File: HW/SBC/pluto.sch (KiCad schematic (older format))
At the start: 0 parts

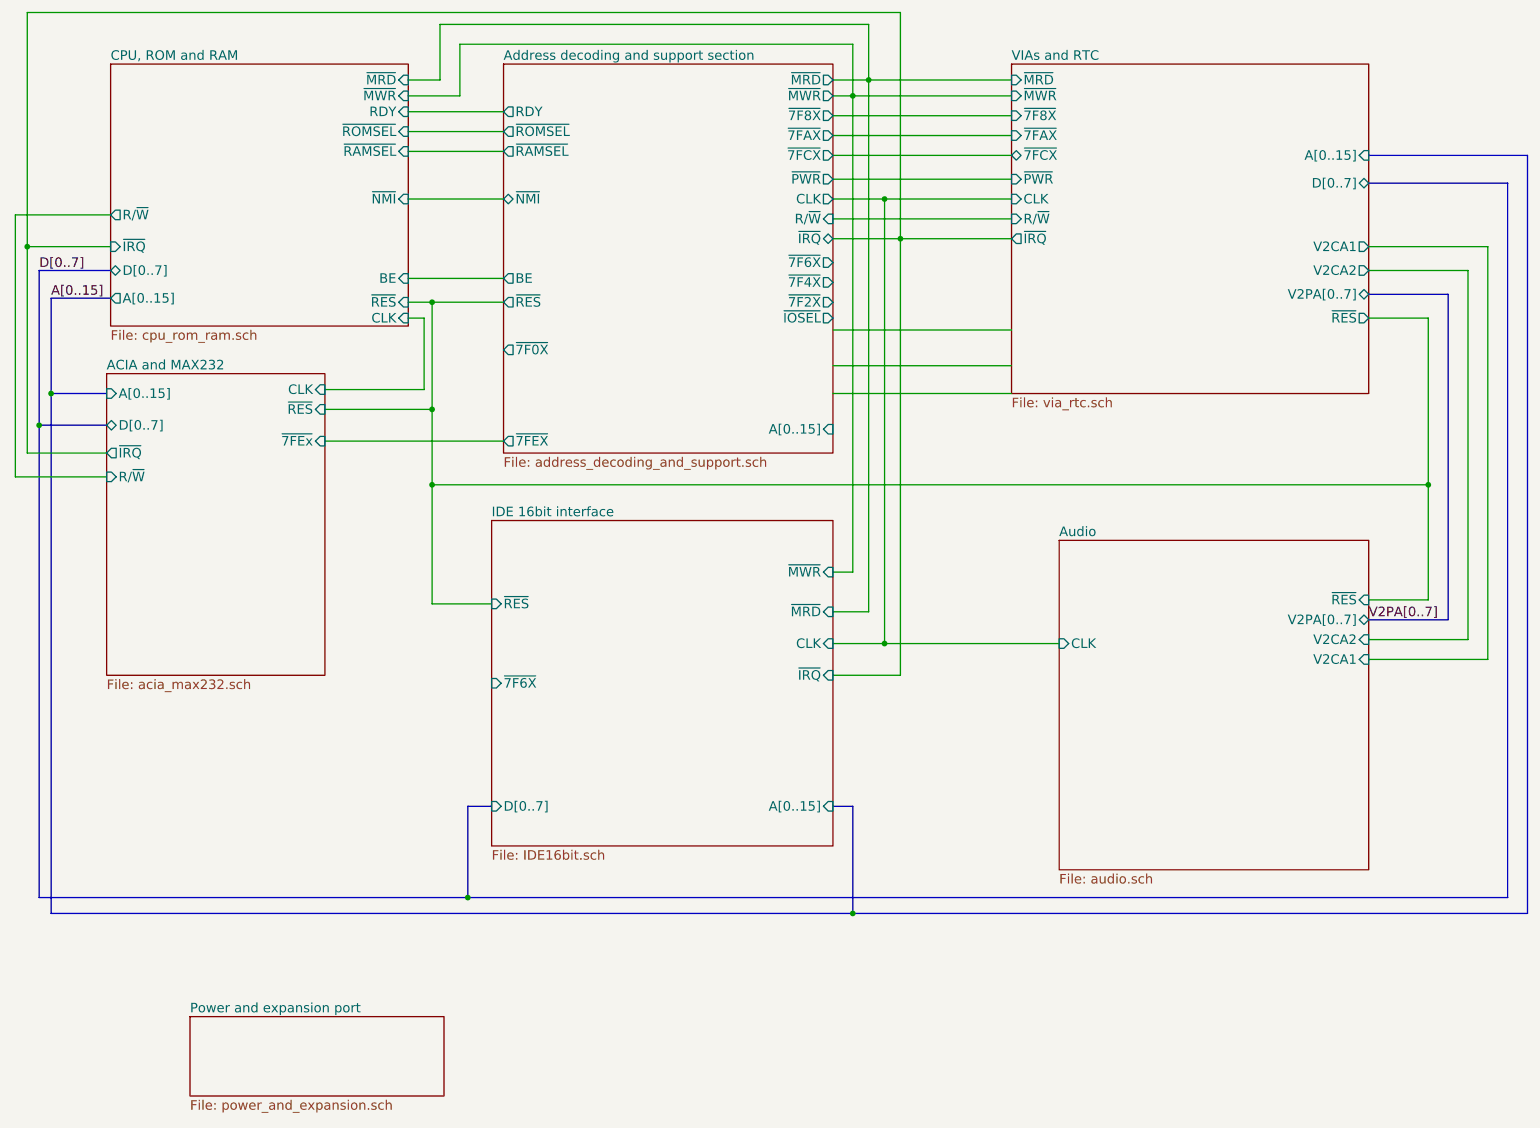
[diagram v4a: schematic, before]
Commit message: Still no VCC net in PCBnew.
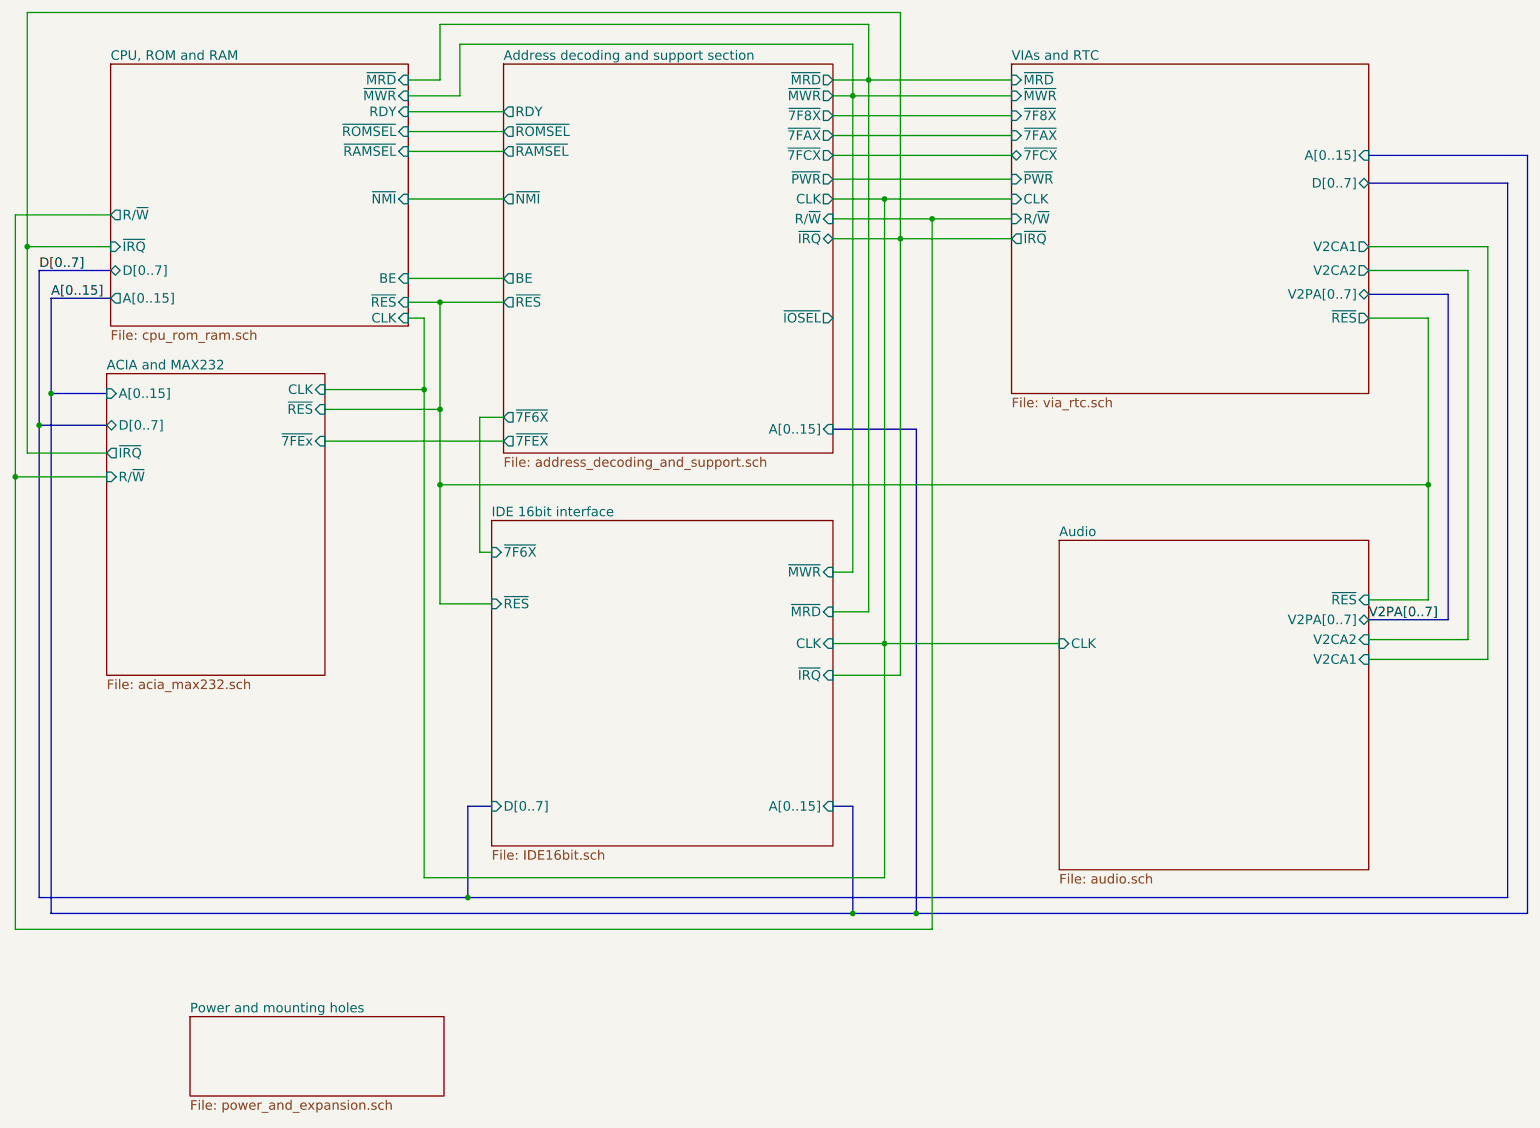
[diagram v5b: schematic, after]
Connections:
- wire segments 56 -> 59
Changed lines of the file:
@@
 EESchema Schematic File Version 2
-LIBS:pluto-rescue
 LIBS:power
 LIBS:device
@@
 LIBS:pluto
 LIBS:pluto-cache
-LIBS:IDE_interface-cache
 EELAYER 25 0
 EELAYER END
@@
 F7 "R/~W" O L 1350 1850 60
 F8 "~NMI" I R 3225 1750 60
-F9 "~RES" I R 3225 2400 60
-F10 "CLK" I R 3225 2500 60
-F11 "~MRD" I R 3225 1000 60
-F12 "~MWR" I R 3225 1100 60
-F13 "~RAMSEL" I R 3225 1450 60
-F14 "~ROMSEL" I R 3225 1325 60
+F9 "CLK" I R 3225 2500 60
+F10 "~MRD" I R 3225 1000 60
+F11 "~MWR" I R 3225 1100 60
+F12 "~RAMSEL" I R 3225 1450 60
+F13 "~ROMSEL" I R 3225 1325 60
+F14 "~RES" I R 3225 2400 60
 $EndSheet
 $Sheet
@@
 F9 "R/~W" I R 5900 1875 60
 F10 "~IRQ" B R 5900 2000 60
-F11 "~NMI" B L 3825 1750 60
+F11 "~NMI" O L 3825 1750 60
 F12 "BE" O L 3825 2250 60
 F13 "~PWR" O R 5900 1625 60
 F14 "RDY" O L 3825 1200 60
 F15 "~RES" O L 3825 2400 60
-F16 "~7F0X" O L 3825 2700 60
-F17 "~7F2X" O R 5900 2400 60
-F18 "~7F4X" O R 5900 2275 60
-F19 "~7F6X" O R 5900 2150 60
-F20 "~7F8X" O R 5900 1225 60
-F21 "~7FAX" O R 5900 1350 60
-F22 "~7FCX" O R 5900 1475 60
-F23 "~7FEX" O L 3825 3275 60
+F16 "~7F6X" O L 3825 3125 60
+F17 "~7F8X" O R 5900 1225 60
+F18 "~7FAX" O R 5900 1350 60
+F19 "~7FCX" O R 5900 1475 60
+F20 "~7FEX" O L 3825 3275 60
 $EndSheet
 $Sheet
 S 1850 6900 1600 500
 U 58D589DC
-F0 "Power and expansion port" 60
+F0 "Power and mounting holes" 60
 F1 "power_and_expansion.sch" 60
 $EndSheet
@@
 F1 "audio.sch" 60
 F2 "V2PA[0..7]" B R 9275 4400 60
-F4 "V2CA2" I R 9275 4525 60
-F5 "V2CA1" I R 9275 4650 60
-F6 "~RES" I R 9275 4275 60
-F7 "CLK" I L 7325 4550 60
-$EndSheet
-Wire Wire Line
-	5900 2800 7025 2800
-Wire Wire Line
-	5900 2975 7025 2975
-Wire Wire Line
-	5900 2575 7025 2575
+F3 "V2CA2" I R 9275 4525 60
+F4 "V2CA1" I R 9275 4650 60
+F5 "~RES" I R 9275 4275 60
+F6 "CLK" I L 7325 4550 60
+$EndSheet
 Wire Wire Line
 	5900 2000 7025 2000
@@
 F6 "CLK" I R 5900 4550 60
 F7 "~MRD" I R 5900 4350 60
-F8 "~7F6X" I L 3750 4800 60
+F8 "~7F6X" I L 3750 3975 60
 F9 "~MWR" I R 5900 4100 60
 $EndSheet
@@
 	3225 2500 3325 2500
 Wire Wire Line
-	3325 2500 3325 2950
+	3325 2500 3325 6025
 Wire Wire Line
 	3325 2950 2700 2950
@@
 	3225 2400 3825 2400
 Wire Wire Line
-	3375 2400 3375 4300
-Wire Wire Line
-	3375 3075 2700 3075
+	3425 2400 3425 4300
+Wire Wire Line
+	3425 3075 2700 3075
 Wire Wire Line
 	3225 2250 3825 2250
@@
 	1350 1850 750  1850
 Wire Wire Line
-	750  1850 750  3500
+	750  1850 750  6350
 Wire Wire Line
 	750  3500 1325 3500
@@
 	5900 4550 7325 4550
 Wire Wire Line
-	6225 1750 6225 4550
+	6225 1750 6225 6025
 Connection ~ 6225 4550
 Connection ~ 6225 1750
@@
 Wire Wire Line
 	6325 4750 5900 4750
-Connection ~ 3375 2400
-Wire Wire Line
-	3375 4300 3750 4300
-Connection ~ 3375 3075
-Wire Wire Line
-	3375 3550 9650 3550
+Connection ~ 3425 2400
+Wire Wire Line
+	3425 4300 3750 4300
+Connection ~ 3425 3075
+Wire Wire Line
+	3425 3550 9650 3550
 Connection ~ 9650 3550
-Connection ~ 3375 3550
+Connection ~ 3425 3550
 Wire Wire Line
 	3225 1750 3825 1750
+Wire Wire Line
+	3825 3125 3675 3125
+Wire Wire Line
+	3675 3125 3675 3975
+Wire Wire Line
+	3675 3975 3750 3975
+Wire Bus Line
+	5900 3200 6425 3200
+Wire Bus Line
+	6425 3200 6425 6250
+Connection ~ 6425 6250
+Wire Wire Line
+	750  6350 6525 6350
+Wire Wire Line
+	6525 6350 6525 1875
+Connection ~ 6525 1875
+Connection ~ 750  3500
+Wire Wire Line
+	6225 6025 3325 6025
+Connection ~ 3325 2950
 $EndSCHEMATC

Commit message: New PCB layout. Added datasheet for AY-3-8912 and LM386.
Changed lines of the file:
@@
 F0 "ACIA and MAX232" 60
 F1 "acia_max232.sch" 60
-F2 "~7FEx" I R 2700 3275 60
+F2 "~7FEX" I R 2700 3275 60
 F3 "R/~W" I L 1325 3500 60
 F4 "~RES" I R 2700 3075 60
@@
 F6 "~ROMSEL" O L 3825 1325 60
 F7 "~RAMSEL" O L 3825 1450 60
-F8 "~IOSEL" O R 5900 2500 60
-F9 "R/~W" I R 5900 1875 60
-F10 "~IRQ" B R 5900 2000 60
-F11 "~NMI" O L 3825 1750 60
-F12 "BE" O L 3825 2250 60
-F13 "~PWR" O R 5900 1625 60
-F14 "RDY" O L 3825 1200 60
-F15 "~RES" O L 3825 2400 60
-F16 "~7F6X" O L 3825 3125 60
-F17 "~7F8X" O R 5900 1225 60
-F18 "~7FAX" O R 5900 1350 60
-F19 "~7FCX" O R 5900 1475 60
-F20 "~7FEX" O L 3825 3275 60
+F8 "R/~W" I R 5900 1875 60
+F9 "~IRQ" B R 5900 2000 60
+F10 "~NMI" O L 3825 1750 60
+F11 "BE" O L 3825 2250 60
+F12 "~PWR" O R 5900 1625 60
+F13 "RDY" O L 3825 1200 60
+F14 "~RES" O L 3825 2400 60
+F15 "~7F6X" O L 3825 3125 60
+F16 "~7F8X" O R 5900 1225 60
+F17 "~7FAX" O R 5900 1350 60
+F18 "~7FCX" O R 5900 1475 60
+F19 "~7FEX" O L 3825 3275 60
 $EndSheet
 $Sheet
@@
 S 3750 3775 2150 2050
 U 5932EBB3
-F0 "IDE 16bit interface" 60
+F0 "16bit IDE interface" 60
 F1 "IDE16bit.sch" 60
 F2 "D[0..7]" I L 3750 5575 60

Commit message: Schema is now Alpha.
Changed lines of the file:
@@
 F13 "~ROMSEL" I R 3225 1325 60
 F14 "~RES" I R 3225 2400 60
+F15 "~SO" I R 3225 1975 60
 $EndSheet
 $Sheet
@@
 F4 "~7FCX" B L 7025 1475 60
 F5 "A[0..15]" I R 9275 1475 60
-F6 "~PWR" I L 7025 1625 60
+F6 "~PWR" O L 7025 1625 60
 F7 "~RES" O R 9275 2500 60
 F8 "~IRQ" O L 7025 2000 60
@@
 F15 "V2CA1" O R 9275 2050 60
 F16 "V2CA2" O R 9275 2200 60
+F17 "~KS" I L 7025 2125 60
 $EndSheet
 $Sheet
@@
 F18 "~7FCX" O R 5900 1475 60
 F19 "~7FEX" O L 3825 3275 60
+F20 "~KS" O R 5900 2125 60
+F21 "~SO" O L 3825 1975 60
 $EndSheet
 $Sheet
@@
 	6225 6025 3325 6025
 Connection ~ 3325 2950
+Wire Wire Line
+	7025 2125 5900 2125
+Wire Wire Line
+	3825 1975 3225 1975
 $EndSCHEMATC
